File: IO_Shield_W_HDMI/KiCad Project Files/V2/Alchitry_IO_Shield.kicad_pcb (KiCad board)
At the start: 4 copper layers, 65 x 45 mm, 72 parts, among them Q1 FDN340P, Q2 FDN340P, Q3 FDN340P, Q4 FDN340P, SW1 SW_DIP_x08, SW2 SW_DIP_x08, U1 Alchitry_Single

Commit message: working on placement
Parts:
- RN1, RN10, RN11, RN19, RN2, RN20, RN21, RN23, RN24, RN3, RN4, RN9: value R_Pack04 -> 1k
- RN13, RN14, RN15, RN16, RN17, RN22, RN7, RN8: value R_Pack04 -> 330
- moved Q3 154.5 mm to (56.0, 23.0), turned to 90 degrees
- moved Q2 145.1 mm to (59.5, 23.0), turned to 90 degrees
- moved Q1 144.6 mm to (63.0, 23.0), turned to 90 degrees
- moved Q4 139.8 mm to (52.5, 23.0), turned to 90 degrees
- moved RN12 130.2 mm to (54.0, 32.0), turned to -90 degrees
- moved RN18 127.4 mm to (46.5, 32.0), turned to -90 degrees
- moved RN13 127.2 mm to (50.0, 32.0)
- moved RN6 119.0 mm to (61.5, 32.0), turned to -90 degrees
- moved AFF4 115.4 mm to (44.5, 32.0), turned to 90 degrees
- moved AFF2 114.8 mm to (59.5, 32.0), turned to 90 degrees
- moved RN22 112.5 mm to (42.5, 32.0)
- moved AFF3 109.8 mm to (52.0, 32.0), turned to 90 degrees
- moved RN7 109.6 mm to (65.0, 32.0)
- moved RN5 103.8 mm to (69.0, 32.0), turned to -90 degrees
- moved RN8 99.1 mm to (57.5, 32.0)
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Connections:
- net Net-(AFF1-Pad4) renamed /LEDs/AFF0_C
- net Net-(AFF2-Pad4) renamed /LEDs/AFF1_C
- net Net-(AFF3-Pad4) renamed /LEDs/AFF2_C
- net Net-(AFF4-Pad4) renamed /LEDs/AFF3_C
- AFF1 pad 1: Net-(AFF1-Pad1) -> /LEDs/AFF0_E
- AFF1 pad 10: Net-(AFF1-Pad10) -> /LEDs/AFF0_G
- AFF1 pad 2: Net-(AFF1-Pad2) -> /LEDs/AFF0_D
- AFF1 pad 5: Net-(AFF1-Pad5) -> /LEDs/AFF0_DP
- AFF1 pad 6: Net-(AFF1-Pad6) -> /LEDs/AFF0_B
- AFF1 pad 7: Net-(AFF1-Pad7) -> /LEDs/AFF0_A
- AFF1 pad 9: Net-(AFF1-Pad9) -> /LEDs/AFF0_F
- AFF2 pad 1: Net-(AFF2-Pad1) -> /LEDs/AFF1_E
- AFF2 pad 10: Net-(AFF2-Pad10) -> /LEDs/AFF1_G
- AFF2 pad 2: Net-(AFF2-Pad2) -> /LEDs/AFF1_D
- AFF2 pad 5: Net-(AFF2-Pad5) -> /LEDs/AFF1_DP
- AFF2 pad 6: Net-(AFF2-Pad6) -> /LEDs/AFF1_B
- AFF2 pad 7: Net-(AFF2-Pad7) -> /LEDs/AFF1_A
- AFF2 pad 9: Net-(AFF2-Pad9) -> /LEDs/AFF1_F
- AFF3 pad 1: Net-(AFF3-Pad1) -> /LEDs/AFF2_E
- AFF3 pad 10: Net-(AFF3-Pad10) -> /LEDs/AFF2_G
- AFF3 pad 2: Net-(AFF3-Pad2) -> /LEDs/AFF2_D
- AFF3 pad 5: Net-(AFF3-Pad5) -> /LEDs/AFF2_DP
- AFF3 pad 6: Net-(AFF3-Pad6) -> /LEDs/AFF2_B
- AFF3 pad 7: Net-(AFF3-Pad7) -> /LEDs/AFF2_A
- AFF3 pad 9: Net-(AFF3-Pad9) -> /LEDs/AFF2_F
- AFF4 pad 1: Net-(AFF4-Pad1) -> /LEDs/AFF3_E
- AFF4 pad 10: Net-(AFF4-Pad10) -> /LEDs/AFF3_G
- AFF4 pad 2: Net-(AFF4-Pad2) -> /LEDs/AFF3_D
- AFF4 pad 5: Net-(AFF4-Pad5) -> /LEDs/AFF3_DP
- AFF4 pad 6: Net-(AFF4-Pad6) -> /LEDs/AFF3_B
- AFF4 pad 7: Net-(AFF4-Pad7) -> /LEDs/AFF3_A
- AFF4 pad 9: Net-(AFF4-Pad9) -> /LEDs/AFF3_F
- Q4 pad 1: /AN2 -> /AN3
- RN12 pad 5: Net-(AFF3-Pad2) -> /LEDs/AFF2_DP
- RN12 pad 7: Net-(AFF3-Pad6) -> /LEDs/AFF2_D
- RN12 pad 8: Net-(AFF3-Pad7) -> /LEDs/AFF2_E
- RN13 pad 5: Net-(AFF3-Pad5) -> /LEDs/AFF2_G
- RN13 pad 6: Net-(AFF3-Pad10) -> /LEDs/AFF2_F
- RN13 pad 7: Net-(AFF3-Pad9) -> /LEDs/AFF2_A
- RN13 pad 8: Net-(AFF3-Pad1) -> /LEDs/AFF2_B
- RN18 pad 5: Net-(AFF4-Pad2) -> /LEDs/AFF3_DP
- RN18 pad 7: Net-(AFF4-Pad6) -> /LEDs/AFF3_D
- RN18 pad 8: Net-(AFF4-Pad7) -> /LEDs/AFF3_E
- RN22 pad 5: Net-(AFF4-Pad5) -> /LEDs/AFF3_G
- RN22 pad 6: Net-(AFF4-Pad10) -> /LEDs/AFF3_F
- RN22 pad 7: Net-(AFF4-Pad9) -> /LEDs/AFF3_A
- RN22 pad 8: Net-(AFF4-Pad1) -> /LEDs/AFF3_B
- RN3 pad 7: no_connect_254 -> (no net)
- RN3 pad 8: no_connect_255 -> (no net)
- RN5 pad 5: Net-(AFF1-Pad2) -> /LEDs/AFF0_DP
- RN5 pad 7: Net-(AFF1-Pad6) -> /LEDs/AFF0_D
- RN5 pad 8: Net-(AFF1-Pad7) -> /LEDs/AFF0_E
- RN6 pad 5: Net-(AFF2-Pad2) -> /LEDs/AFF1_DP
- RN6 pad 7: Net-(AFF2-Pad6) -> /LEDs/AFF1_D
- RN6 pad 8: Net-(AFF2-Pad7) -> /LEDs/AFF1_E
- RN7 pad 5: Net-(AFF1-Pad5) -> /LEDs/AFF0_G
- RN7 pad 6: Net-(AFF1-Pad10) -> /LEDs/AFF0_F
- RN7 pad 7: Net-(AFF1-Pad9) -> /LEDs/AFF0_A
- RN7 pad 8: Net-(AFF1-Pad1) -> /LEDs/AFF0_B
- RN8 pad 5: Net-(AFF2-Pad5) -> /LEDs/AFF1_G
- RN8 pad 6: Net-(AFF2-Pad10) -> /LEDs/AFF1_F
- RN8 pad 7: Net-(AFF2-Pad9) -> /LEDs/AFF1_A
- RN8 pad 8: Net-(AFF2-Pad1) -> /LEDs/AFF1_B
- U1 pad A_11: /LED25 -> /LED21
- U1 pad A_12: /LED24 -> /LED32
- U1 pad A_14: /LED23 -> /LED26
- U1 pad A_15: /LED22 -> /LED20
- U1 pad A_17: /LED21 -> /LED31
- U1 pad A_18: /LED20 -> /LED25
- U1 pad A_2: /LED31 -> /LED23
- U1 pad A_21: /LED18 -> /LED30
- U1 pad A_23: /LED17 -> /LED24
- U1 pad A_24: /LED16 -> /LED18
- U1 pad A_27: /LED32 -> (no net)
- U1 pad A_28: /LED33 -> (no net)
- U1 pad A_3: /LED30 -> /LED34
- U1 pad A_30: /LED34 -> (no net)
- U1 pad A_31: /LED35 -> (no net)
- U1 pad A_33: Net-(U1-PadA_33) -> (no net)
- U1 pad A_34: Net-(U1-PadA_34) -> (no net)
- U1 pad A_36: Net-(U1-PadA_36) -> (no net)
- U1 pad A_37: Net-(U1-PadA_37) -> (no net)
- U1 pad A_39: Net-(U1-PadA_39) -> (no net)
- U1 pad A_40: Net-(U1-PadA_40) -> (no net)
- U1 pad A_42: /AN1 -> (no net)
- U1 pad A_43: /AN0 -> (no net)
- U1 pad A_45: /C4 -> (no net)
- U1 pad A_46: /C3 -> (no net)
- U1 pad A_48: /C2 -> /LED29
- U1 pad A_49: /DP -> /LED35
- U1 pad A_5: /LED29 -> /LED28
- U1 pad A_6: /LED28 -> /LED22
- U1 pad A_8: /LED27 -> /LED33
- U1 pad A_9: /LED26 -> /LED27
- U1 pad B_11: Net-(U1-PadB_11) -> /AN1
- U1 pad B_12: Net-(U1-PadB_12) -> /AN0
- U1 pad B_14: Net-(U1-PadB_14) -> /DP
- U1 pad B_15: Net-(U1-PadB_15) -> /C6
- U1 pad B_17: Net-(U1-PadB_17) -> /C5
- U1 pad B_18: Net-(U1-PadB_18) -> /C4
- U1 pad B_2: Net-(U1-PadB_2) -> (no net)
- U1 pad B_20: Net-(U1-PadB_20) -> /C0
- U1 pad B_21: Net-(U1-PadB_21) -> /C1
- U1 pad B_23: Net-(U1-PadB_23) -> /C2
- U1 pad B_24: Net-(U1-PadB_24) -> /C3
- U1 pad B_27: Net-(U1-PadB_27) -> (no net)
- U1 pad B_28: Net-(U1-PadB_28) -> (no net)
- U1 pad B_3: Net-(U1-PadB_3) -> (no net)
- U1 pad B_30: Net-(U1-PadB_30) -> (no net)
- U1 pad B_31: Net-(U1-PadB_31) -> (no net)
- U1 pad B_33: Net-(U1-PadB_33) -> (no net)
- U1 pad B_34: Net-(U1-PadB_34) -> (no net)
- U1 pad B_36: Net-(U1-PadB_36) -> (no net)
- U1 pad B_37: Net-(U1-PadB_37) -> (no net)
- U1 pad B_39: Net-(U1-PadB_39) -> (no net)
- U1 pad B_40: Net-(U1-PadB_40) -> (no net)
- U1 pad B_42: Net-(U1-PadB_42) -> (no net)
- U1 pad B_43: Net-(U1-PadB_43) -> (no net)
- U1 pad B_45: Net-(U1-PadB_45) -> (no net)
- U1 pad B_46: Net-(U1-PadB_46) -> (no net)
- U1 pad B_48: Net-(U1-PadB_48) -> (no net)
- U1 pad B_49: Net-(U1-PadB_49) -> (no net)
- U1 pad B_5: Net-(U1-PadB_5) -> (no net)
- U1 pad B_6: Net-(U1-PadB_6) -> (no net)
- U1 pad B_8: Net-(U1-PadB_8) -> /AN3
- U1 pad B_9: Net-(U1-PadB_9) -> /AN2
- U1 pad C_1: Net-(U1-PadC_1) -> +5V
- U1 pad C_11: Net-(U1-PadC_11) -> (no net)
- U1 pad C_12: Net-(U1-PadC_12) -> (no net)
- U1 pad C_13: Net-(U1-PadC_13) -> +3V3
- U1 pad C_14: Net-(U1-PadC_14) -> (no net)
- U1 pad C_15: Net-(U1-PadC_15) -> (no net)
- U1 pad C_17: Net-(U1-PadC_17) -> (no net)
- U1 pad C_18: Net-(U1-PadC_18) -> (no net)
- U1 pad C_19: Net-(U1-PadC_13) -> +3V3
- U1 pad C_2: Net-(U1-PadC_2) -> /LED11
- U1 pad C_20: Net-(U1-PadC_20) -> (no net)
- U1 pad C_21: Net-(U1-PadC_21) -> (no net)
- U1 pad C_23: Net-(U1-PadC_23) -> (no net)
- U1 pad C_24: Net-(U1-PadC_24) -> (no net)
- U1 pad C_25: Net-(U1-PadC_25) -> (no net)
- U1 pad C_27: /LED0 -> /LED12
- U1 pad C_28: /LED1 -> /LED6
- U1 pad C_3: Net-(U1-PadC_3) -> /LED5
- U1 pad C_30: /LED2 -> /LED0
- U1 pad C_31: /LED3 -> /LED13
- U1 pad C_33: /LED4 -> /LED7
- U1 pad C_34: /LED5 -> /LED1
- U1 pad C_36: /LED6 -> /LED14
- U1 pad C_37: /LED7 -> /LED8
- U1 pad C_39: /LED8 -> /LED2
- U1 pad C_40: /LED9 -> /LED15
- U1 pad C_42: /LED10 -> /LED9
- U1 pad C_43: /LED11 -> /LED3
- U1 pad C_45: /LED12 -> /LED16
- U1 pad C_46: /LED13 -> /LED10
- U1 pad C_48: /LED14 -> /LED4
- U1 pad C_49: /LED15 -> /LED17
- U1 pad C_5: Net-(U1-PadC_5) -> (no net)
- U1 pad C_6: Net-(U1-PadC_6) -> (no net)
- U1 pad C_7: Net-(U1-PadC_13) -> +3V3
- U1 pad C_8: Net-(U1-PadC_8) -> (no net)
- U1 pad C_9: Net-(U1-PadC_9) -> (no net)
- U1 pad D_1: no_connect_256 -> (no net)
- U1 pad D_11: no_connect_257 -> (no net)
- U1 pad D_12: no_connect_258 -> (no net)
- U1 pad D_14: no_connect_259 -> (no net)
- U1 pad D_15: no_connect_260 -> (no net)
- U1 pad D_17: no_connect_261 -> (no net)
- U1 pad D_18: no_connect_262 -> (no net)
- U1 pad D_2: no_connect_263 -> (no net)
- U1 pad D_20: no_connect_264 -> (no net)
- U1 pad D_21: no_connect_265 -> (no net)
- U1 pad D_23: no_connect_266 -> (no net)
- U1 pad D_24: no_connect_267 -> (no net)
- U1 pad D_27: no_connect_268 -> (no net)
- U1 pad D_28: no_connect_269 -> (no net)
- U1 pad D_3: no_connect_270 -> (no net)
- U1 pad D_30: no_connect_271 -> (no net)
- U1 pad D_31: no_connect_272 -> (no net)
- U1 pad D_33: no_connect_273 -> (no net)
- U1 pad D_34: no_connect_274 -> (no net)
- U1 pad D_36: no_connect_275 -> (no net)
- U1 pad D_37: no_connect_276 -> (no net)
- U1 pad D_39: no_connect_277 -> (no net)
- U1 pad D_40: no_connect_278 -> (no net)
- U1 pad D_42: no_connect_279 -> (no net)
- U1 pad D_43: no_connect_280 -> (no net)
- U1 pad D_45: Net-(U1-PadD_45) -> (no net)
- U1 pad D_46: Net-(U1-PadD_46) -> (no net)
- U1 pad D_48: Net-(U1-PadD_48) -> (no net)
- U1 pad D_49: Net-(U1-PadD_49) -> (no net)
- U1 pad D_5: no_connect_281 -> (no net)
- U1 pad D_50: no_connect_282 -> (no net)
- U1 pad D_6: no_connect_283 -> (no net)
- U1 pad D_8: no_connect_284 -> (no net)
- U1 pad D_9: no_connect_285 -> (no net)
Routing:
- net /LED12: track 60.8 -> 1.44 mm
- net /LED6: track 56.5 -> 1.44 mm
- net /LED7: track 56.4 -> 1.44 mm
- net /LED13: track 54.5 -> 1.44 mm
- net /LED8: track 52.5 -> 1.44 mm
- net /LED14: track 50.8 -> 1.44 mm
- net /LED15: track 50.3 -> 1.44 mm
- net /LED9: track 46.0 -> 1.44 mm
- net /LED11: track 42.8 -> 1.44 mm
- net /LED10: track 42.4 -> 1.44 mm
- net /LED5: track 33.5 -> 1.44 mm
- net /LED4: track 33.1 -> 1.44 mm
- net /C6: track 0.00 -> 30.8 mm, vias 0 -> 5
- net /DP: track 1.44 -> 32.1 mm, vias 1 -> 5
- net /C1: track 0.00 -> 30.2 mm, vias 0 -> 1
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- added copper zone on F.Cu, net GNDREF
- removed copper zone on F.Cu, net +3V3

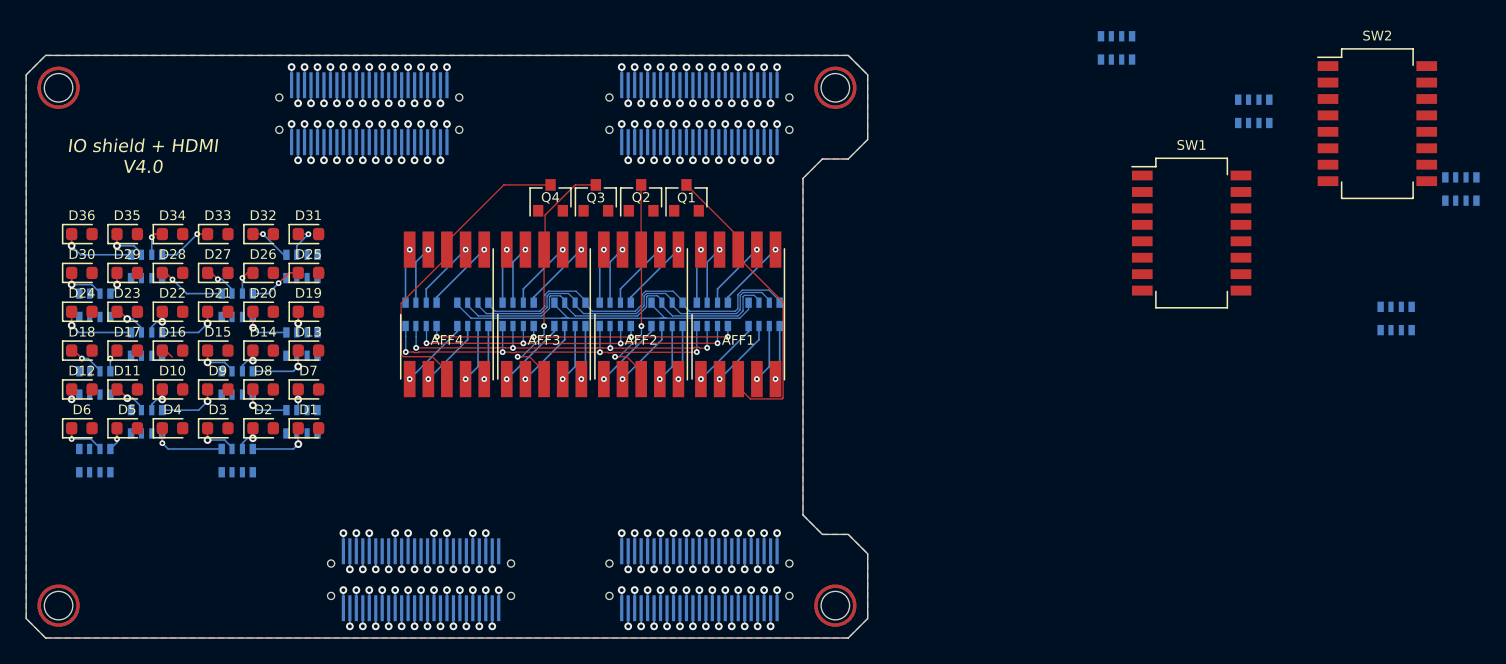
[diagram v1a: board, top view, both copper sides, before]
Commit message: switches and 7seg routed
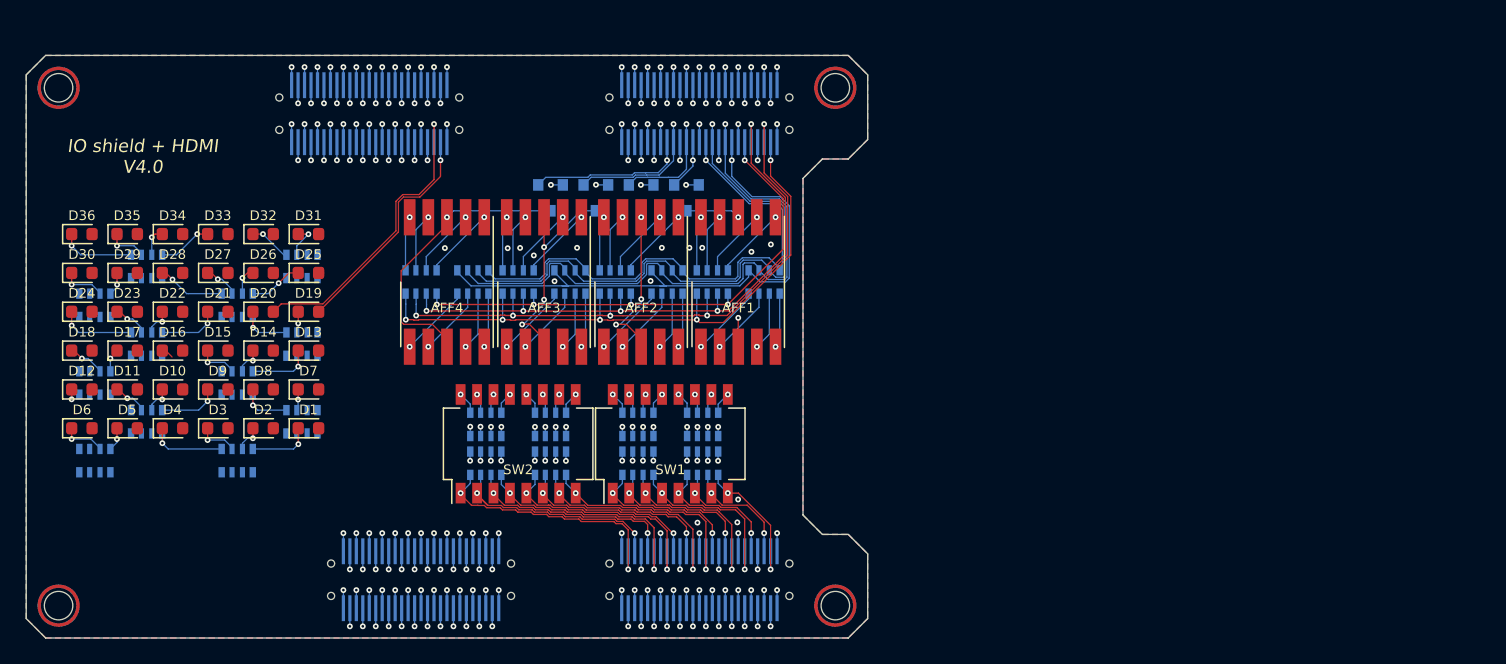
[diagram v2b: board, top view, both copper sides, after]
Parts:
- added RN25: 330, Resistor_SMD:R_Array_Convex_4x0603, B.Cu at (64.2, 43.5)
- added RN26: 330, Resistor_SMD:R_Array_Convex_4x0603, B.Cu at (59.2, 43.5)
- added RN27: 330, Resistor_SMD:R_Array_Convex_4x0603, B.Cu at (52.5, 43.5)
- added RN28: 1k, Resistor_SMD:R_Array_Convex_4x0603, B.Cu at (47.5, 43.5)
- Q1, Q2, Q3, Q4: moved to B.Cu
- moved RN16 72.6 mm to (52.5, 40.5)
- moved SW2 70.8 mm to (50.0, 42.0), turned to 90 degrees
- moved RN17 70.8 mm to (47.5, 40.5)
- moved RN15 53.4 mm to (59.2, 40.5)
- moved SW1 43.4 mm to (61.8, 42.0), turned to 90 degrees
- moved RN14 43.2 mm to (64.2, 40.5)
- moved AFF1 2.50 mm to (67.0, 29.5)
- moved AFF2 2.50 mm to (59.5, 29.5)
- moved AFF3 2.50 mm to (52.0, 29.5)
- moved AFF4 2.50 mm to (44.5, 29.5)
- moved RN12 2.50 mm to (54.0, 29.5)
- moved RN13 2.50 mm to (50.0, 29.5)
- moved RN18 2.50 mm to (46.5, 29.5)
- moved RN22 2.50 mm to (42.5, 29.5)
- moved RN5 2.50 mm to (69.0, 29.5)
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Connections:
- D26 pad 2: /LED25 -> (no net)
- D27 pad 2: /LED26 -> (no net)
- D28 pad 2: /LED27 -> (no net)
- D29 pad 2: /LED28 -> (no net)
- D31 pad 2: /LED30 -> (no net)
- D32 pad 2: /LED31 -> (no net)
- D33 pad 2: /LED32 -> (no net)
- D34 pad 2: /LED33 -> (no net)
- D35 pad 2: /LED34 -> (no net)
- SW1 pad 1: (no net) -> /DIP7
- SW1 pad 2: (no net) -> /DIP6
- SW1 pad 3: (no net) -> /DIP5
- SW1 pad 4: (no net) -> /DIP4
- SW1 pad 5: (no net) -> /DIP3
- SW1 pad 6: (no net) -> /DIP2
- SW1 pad 7: (no net) -> /DIP1
- SW1 pad 8: (no net) -> /DIP0
- SW2 pad 1: (no net) -> /DIP15
- SW2 pad 2: (no net) -> /DIP14
- SW2 pad 3: (no net) -> /DIP13
- SW2 pad 4: (no net) -> /DIP12
- SW2 pad 5: (no net) -> /DIP11
- SW2 pad 6: (no net) -> /DIP10
- SW2 pad 7: (no net) -> /DIP9
- SW2 pad 8: (no net) -> /DIP8
- U1 pad A_11: /LED21 -> (no net)
- U1 pad A_12: /LED32 -> (no net)
- U1 pad A_14: /LED26 -> (no net)
- U1 pad A_15: /LED20 -> /LED24
- U1 pad A_17: /LED31 -> /LED23
- U1 pad A_18: /LED25 -> /LED22
- U1 pad A_2: /LED23 -> (no net)
- U1 pad A_20: /LED19 -> /LED21
- U1 pad A_21: /LED30 -> /LED20
- U1 pad A_23: /LED24 -> /LED19
- U1 pad A_3: /LED34 -> (no net)
- U1 pad A_5: /LED28 -> (no net)
- U1 pad A_6: /LED22 -> (no net)
- U1 pad A_8: /LED33 -> (no net)
- U1 pad A_9: /LED27 -> (no net)
- U1 pad B_14: /DP -> /C3
- U1 pad B_15: /C6 -> /C2
- U1 pad B_17: /C5 -> /C1
- U1 pad B_18: /C4 -> /C0
- U1 pad B_20: /C0 -> /C4
- U1 pad B_21: /C1 -> /C5
- U1 pad B_23: /C2 -> /C6
- U1 pad B_24: /C3 -> /DP
- U1 pad D_27: (no net) -> /DIP0
- U1 pad D_28: (no net) -> /DIP1
- U1 pad D_30: (no net) -> /DIP2
- U1 pad D_31: (no net) -> /DIP3
- U1 pad D_33: (no net) -> /DIP4
- U1 pad D_34: (no net) -> /DIP5
- U1 pad D_36: (no net) -> /DIP6
- U1 pad D_37: (no net) -> /DIP7
- U1 pad D_39: (no net) -> /DIP8
- U1 pad D_40: (no net) -> /DIP9
- U1 pad D_42: (no net) -> /DIP10
- U1 pad D_43: (no net) -> /DIP11
- U1 pad D_45: (no net) -> /DIP12
- U1 pad D_46: (no net) -> /DIP13
- U1 pad D_48: (no net) -> /DIP14
- U1 pad D_49: (no net) -> /DIP15
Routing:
- net /LED19: track 1.44 -> 23.7 mm
- net +3V3: track 40.0 -> 61.0 mm, vias 28 -> 52
- net /DIP15: track 0.00 -> 20.4 mm, vias 0 -> 2
- net /C6: track 30.8 -> 49.8 mm
- net /DIP12: track 0.00 -> 18.6 mm, vias 0 -> 2
- net /DIP11: track 0.00 -> 18.2 mm, vias 0 -> 2
- net /C5: track 29.3 -> 47.4 mm
- net /DIP14: track 0.00 -> 17.8 mm, vias 0 -> 2
- net /DP: track 32.1 -> 49.6 mm
- net /DIP13: track 0.00 -> 16.6 mm, vias 0 -> 2
- net /DIP8: track 0.00 -> 16.5 mm, vias 0 -> 2
- net /LED18: track 1.44 -> 17.8 mm
- net /C1: track 30.2 -> 46.4 mm
- net /C0: track 29.7 -> 45.6 mm
- net /C2: track 30.2 -> 45.6 mm
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
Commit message: routing complete... ,maybe add button
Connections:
- D26 pad 2: (no net) -> /LED25
- D27 pad 2: (no net) -> /LED26
- D28 pad 2: (no net) -> /LED27
- D29 pad 2: (no net) -> /LED28
- D31 pad 2: (no net) -> /LED30
- D32 pad 2: (no net) -> /LED31
- D33 pad 2: (no net) -> /LED32
- D34 pad 2: (no net) -> /LED33
- D35 pad 2: (no net) -> /LED34
- U1 pad A_1: +5V -> (no net)
- U1 pad A_11: (no net) -> /LED27
- U1 pad A_12: (no net) -> /LED26
- U1 pad A_14: (no net) -> /LED25
- U1 pad A_2: (no net) -> /LED33
- U1 pad A_3: (no net) -> /LED32
- U1 pad A_48: /LED29 -> /LED34
- U1 pad A_5: (no net) -> /LED31
- U1 pad A_50: +5V -> (no net)
- U1 pad A_6: (no net) -> /LED30
- U1 pad A_8: (no net) -> /LED29
- U1 pad A_9: (no net) -> /LED28
- U1 pad B_1: +5V -> (no net)
- U1 pad B_50: +5V -> (no net)
- U1 pad C_1: +5V -> (no net)
- U1 pad C_2: /LED11 -> /LED12
- U1 pad C_27: /LED12 -> /LED14
- U1 pad C_28: /LED6 -> /LED15
- U1 pad C_3: /LED5 -> /LED13
- U1 pad C_30: /LED0 -> /LED16
- U1 pad C_31: /LED13 -> /LED17
- U1 pad C_33: /LED7 -> /LED6
- U1 pad C_34: /LED1 -> /LED7
- U1 pad C_36: /LED14 -> /LED8
- U1 pad C_37: /LED8 -> /LED9
- U1 pad C_39: /LED2 -> /LED10
- U1 pad C_40: /LED15 -> /LED11
- U1 pad C_42: /LED9 -> /LED0
- U1 pad C_43: /LED3 -> /LED1
- U1 pad C_45: /LED16 -> /LED2
- U1 pad C_46: /LED10 -> /LED3
- U1 pad C_49: /LED17 -> /LED5
- U1 pad C_50: +5V -> (no net)
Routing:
- net /LED12: track 1.44 -> 59.8 mm
- net /LED13: track 1.44 -> 53.2 mm
- net /LED17: track 1.44 -> 39.9 mm
- net /LED23: track 1.44 -> 35.2 mm
- net /LED16: track 1.44 -> 34.1 mm
- net /LED11: track 1.44 -> 32.4 mm
- net /LED15: track 1.44 -> 31.6 mm
- net /LED14: track 1.44 -> 31.4 mm
- net /LED10: track 1.44 -> 31.4 mm
- net /LED5: track 1.44 -> 30.5 mm
- net /LED22: track 1.44 -> 29.2 mm
- net /LED9: track 1.44 -> 29.0 mm
- net /LED28: track 0.00 -> 27.3 mm, vias 0 -> 1
- net /LED29: track 1.44 -> 27.7 mm
- net /LED34: track 0.00 -> 25.9 mm, vias 0 -> 1
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
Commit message: layout again
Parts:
- moved D20 1.96 mm to (29.5, 30.0)
- moved D21 1.96 mm to (26.0, 30.0)
- moved D22 1.96 mm to (22.5, 30.0)
- moved D23 1.96 mm to (19.0, 30.0)
- moved D24 1.96 mm to (15.5, 30.0)
- moved D26 1.96 mm to (29.5, 27.0)
- moved D27 1.96 mm to (26.0, 27.0)
- moved D28 1.96 mm to (22.5, 27.0)
- moved D29 1.96 mm to (19.0, 27.0)
- moved D30 1.96 mm to (15.5, 27.0)
- moved D32 1.96 mm to (29.5, 24.0)
- moved D33 1.96 mm to (26.0, 24.0)
- moved D34 1.96 mm to (22.5, 24.0)
- moved D35 1.96 mm to (19.0, 24.0)
- moved D36 1.96 mm to (15.5, 24.0)
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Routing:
- net /LED6: track 19.7 -> 5.62 mm
- net /LED17: track 39.9 -> 26.5 mm
- net /LED16: track 34.1 -> 20.8 mm
- net /LED7: track 19.5 -> 6.39 mm
- net /LED14: track 31.4 -> 18.4 mm
- net /LED15: track 31.6 -> 18.7 mm
- net /LED8: track 22.5 -> 10.6 mm
- net /LED9: track 29.0 -> 17.8 mm
- net /LED10: track 31.4 -> 21.5 mm
- net /LED11: track 32.4 -> 23.1 mm
- net /LED0: track 12.4 -> 5.07 mm
- net /LED1: track 18.2 -> 20.4 mm
- net /LED2: track 21.2 -> 23.3 mm
- net /LED3: track 21.6 -> 23.7 mm
- net /LED4: track 24.6 -> 26.6 mm
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
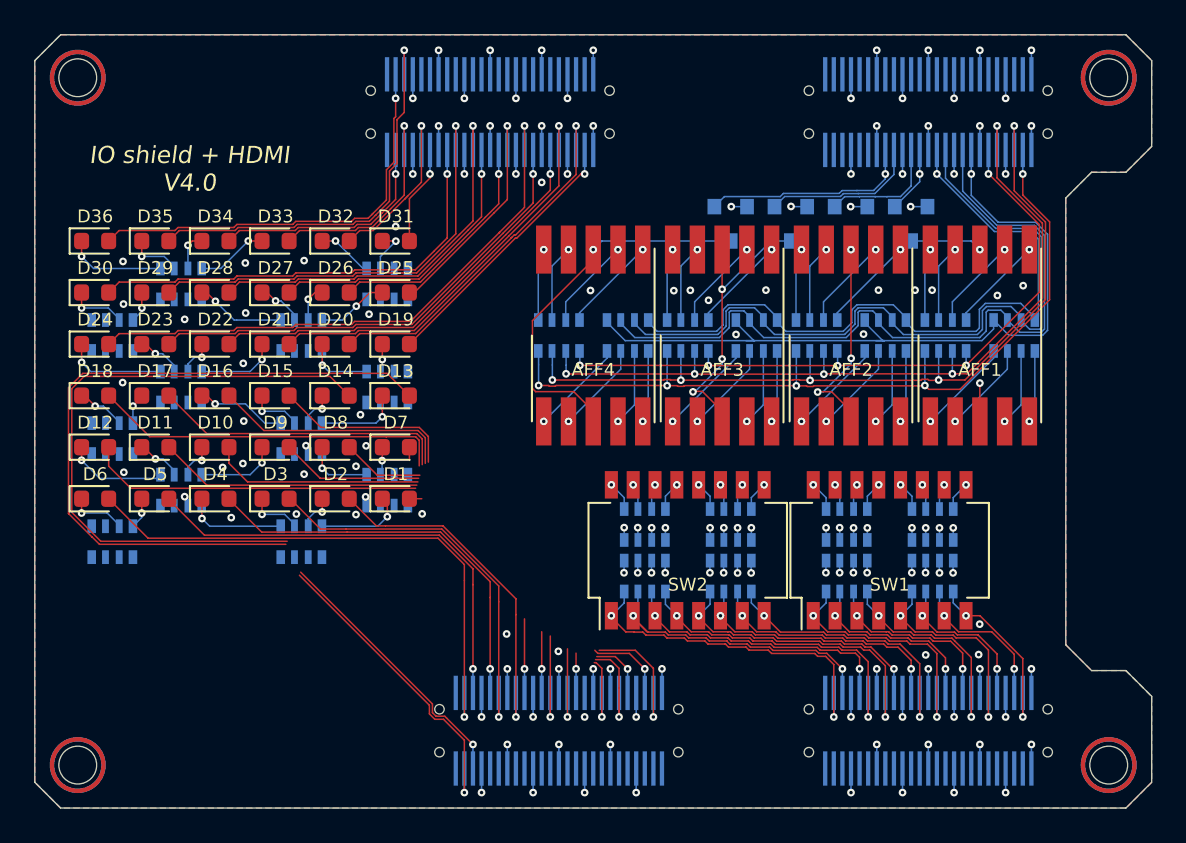
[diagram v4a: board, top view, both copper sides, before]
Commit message: added push butttons
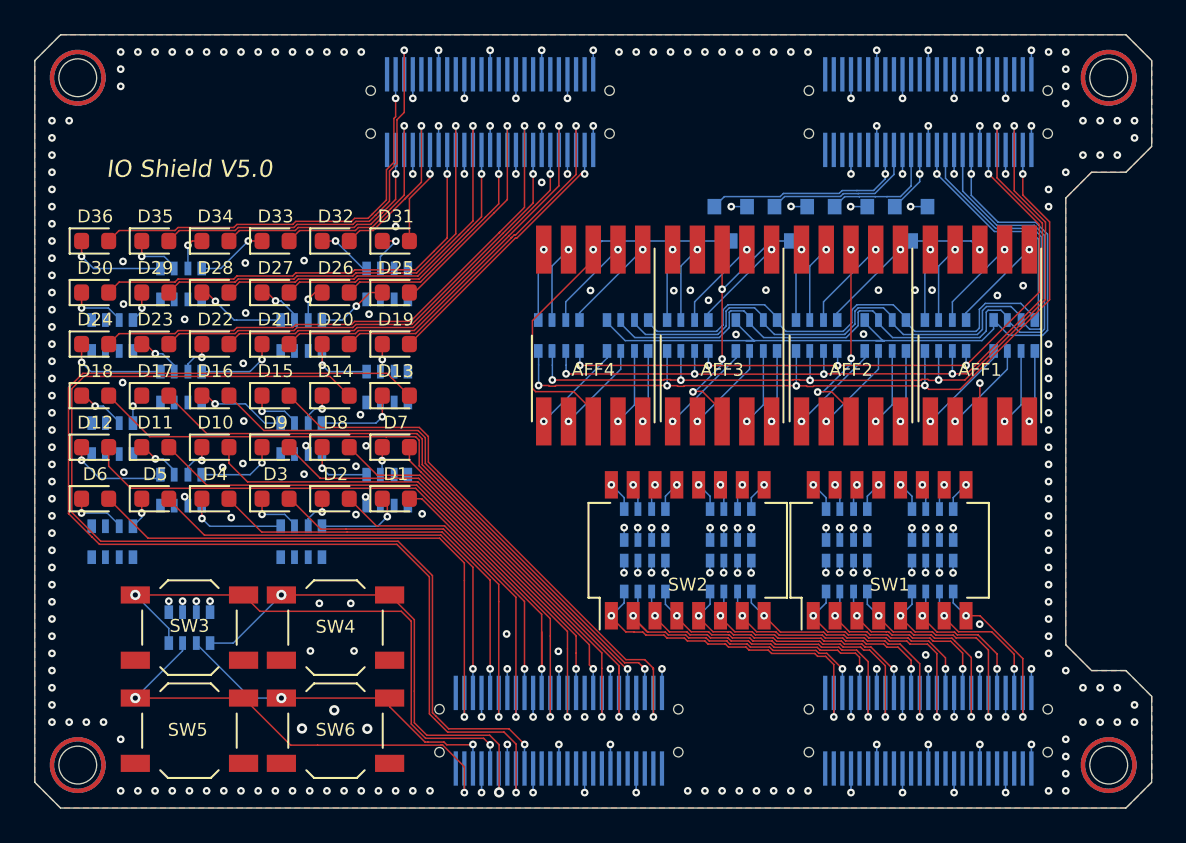
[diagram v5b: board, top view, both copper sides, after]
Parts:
- added RN29: 1k, Resistor_SMD:R_Array_Convex_4x0603, B.Cu at (21.0, 46.5)
- added SW3: SW_Push, Button_Switch_SMD:SW_SPST_TL3342, F.Cu at (21.0, 46.5)
- added SW4: SW_Push, Button_Switch_SMD:SW_SPST_TL3342, F.Cu at (29.5, 46.5)
- added SW5: SW_Push, Button_Switch_SMD:SW_SPST_TL3342, F.Cu at (21.0, 52.5)
- added SW6: SW_Push, Button_Switch_SMD:SW_SPST_TL3342, F.Cu at (29.5, 52.5)
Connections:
- U1 pad C_2: /LED12 -> /btn2
- U1 pad C_3: /LED13 -> /btn3
- U1 pad C_5: (no net) -> /btn0
- U1 pad C_6: (no net) -> /btn1
- U1 pad C_8: (no net) -> /LED12
- U1 pad C_9: (no net) -> /LED13
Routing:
- net /btn0: track 0.00 -> 32.8 mm, vias 0 -> 2
- net /btn1: track 0.00 -> 29.3 mm, vias 0 -> 2
- net /btn2: track 0.00 -> 28.1 mm, vias 0 -> 2
- net /btn3: track 0.00 -> 20.3 mm, vias 0 -> 2
- net /LED6: track 5.62 -> 21.8 mm
- net /LED7: track 6.39 -> 21.8 mm
- net /LED17: track 26.5 -> 41.8 mm
- net /LED16: track 20.8 -> 35.6 mm
- net /LED14: track 18.4 -> 33.0 mm
- net /LED15: track 18.7 -> 33.1 mm
- net /LED8: track 10.6 -> 24.6 mm
- net /LED11: track 23.1 -> 36.7 mm
- net /LED9: track 17.8 -> 31.1 mm
- net /LED10: track 21.5 -> 33.5 mm
- net /LED0: track 5.07 -> 14.5 mm
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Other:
- board text added: "IO Shield V5.0"
- board text removed: "IO shield + HDMI V4.0"
